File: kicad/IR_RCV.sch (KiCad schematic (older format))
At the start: 15 parts, among them P5 PR_Host, P6 PR_Slave, Q1 DMN3065LW-7, U6 TLV316IDCKR

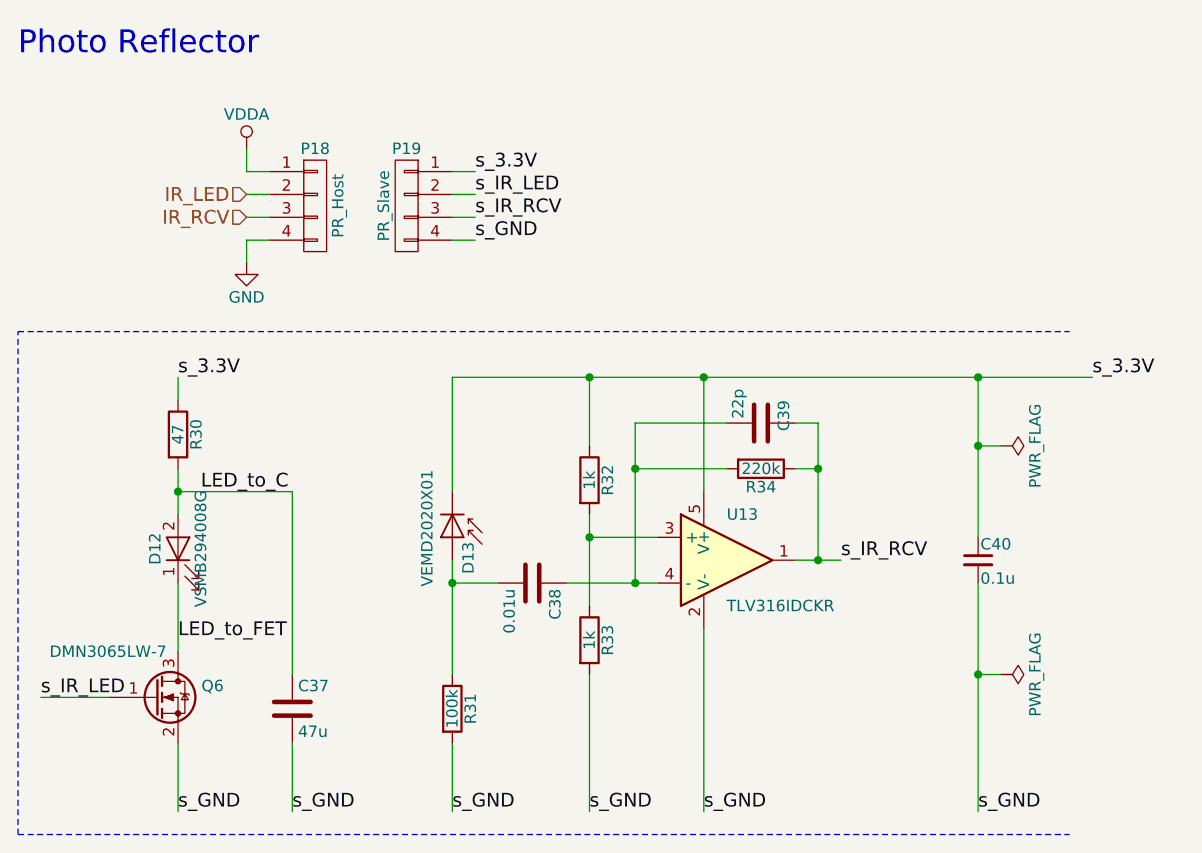
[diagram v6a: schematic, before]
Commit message: 実装経験をもとにフットプリントを改良，ミスを修正
SC70サイズのオペアンプのピンアサインを修正
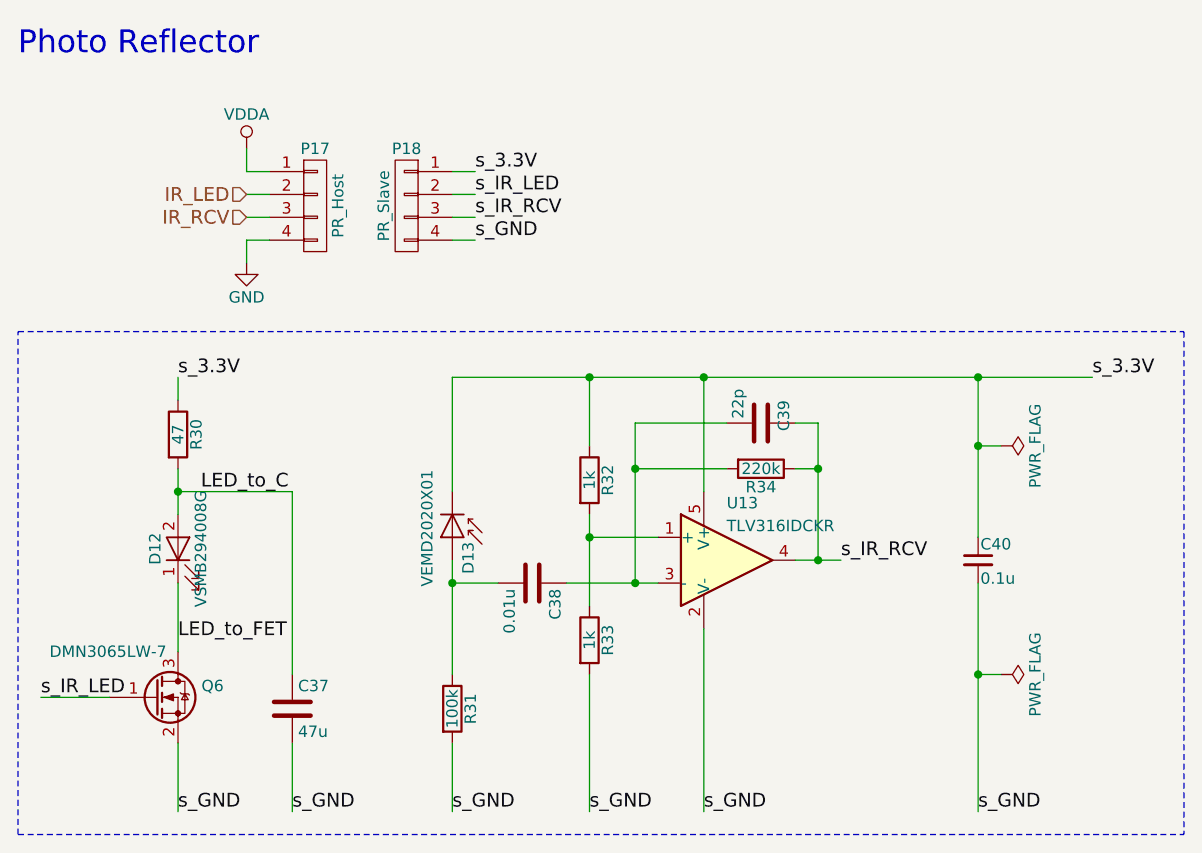
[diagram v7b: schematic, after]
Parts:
- removed U6: TLV316IDCKR, TO_SOT_Packages_SMD:SOT-353_SC-70-5, symbol MCP6L91
- added U6: TLV316IDCKR, TO_SOT_Packages_SMD:SOT-353_SC-70-5, symbol OPA333DCK
- renumbered P5 to P4, P6 to P5
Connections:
- net s_3.3V: now also U6.5 (V+)
- net s_GND: now also U6.2 (V-)
- net s_IR_RCV: now also U6.4
- net at C20.1, C21.2, R10.2: now also U6.3 (-)
- net at R8.2, R9.1: now also U6.1 (+)
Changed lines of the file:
@@
 Photo Reflector
 $Comp
-L CONN_01X04 P6
+L CONN_01X04 P5
 U 1 1 589BE652
 P 5400 2550
-AR Path="/57CF0B09/589BE652" Ref="P6"  Part="1"
-AR Path="/57CF2A30/589BE652" Ref="P8"  Part="1"
-AR Path="/597E1B35/589BE652" Ref="P17"  Part="1"
-AR Path="/597E1B39/589BE652" Ref="P19"  Part="1"
-F 0 "P19" H 5400 2800 50  0000 C CNN
+AR Path="/57CF0B09/589BE652" Ref="P5"  Part="1"
+AR Path="/57CF2A30/589BE652" Ref="P7"  Part="1"
+AR Path="/597E1B35/589BE652" Ref="P16"  Part="1"
+AR Path="/597E1B39/589BE652" Ref="P18"  Part="1"
+F 0 "P18" H 5400 2800 50  0000 C CNN
 F 1 "PR_Slave" V 5500 2550 50  0000 C CNN
 F 2 "mouse:STAND_PR_SLAVE" H 5400 2550 50  0001 C CNN
@@
 s_IR_LED
 $Comp
-L CONN_01X04 P5
+L CONN_01X04 P4
 U 1 1 589BE88F
 P 5000 2550
-AR Path="/57CF0B09/589BE88F" Ref="P5"  Part="1"
-AR Path="/57CF2A30/589BE88F" Ref="P7"  Part="1"
-AR Path="/597E1B35/589BE88F" Ref="P16"  Part="1"
-AR Path="/597E1B39/589BE88F" Ref="P18"  Part="1"
-F 0 "P18" H 5000 2800 50  0000 C CNN
+AR Path="/57CF0B09/589BE88F" Ref="P4"  Part="1"
+AR Path="/57CF2A30/589BE88F" Ref="P6"  Part="1"
+AR Path="/597E1B35/589BE88F" Ref="P15"  Part="1"
+AR Path="/597E1B39/589BE88F" Ref="P17"  Part="1"
+F 0 "P17" H 5000 2800 50  0000 C CNN
 F 1 "PR_Host" V 5100 2550 50  0000 C CNN
 F 2 "mouse:STAND_PR_HOST" H 5000 2550 50  0001 C CNN
@@
 IR_LED
 $Comp
-L GND #PWR043
+L GND #PWR42
 U 1 1 589BF265
 P 4700 2800
-AR Path="/57CF0B09/589BF265" Ref="#PWR043"  Part="1"
-AR Path="/57CF2A30/589BF265" Ref="#PWR047"  Part="1"
-AR Path="/597E1B35/589BF265" Ref="#PWR080"  Part="1"
-AR Path="/597E1B39/589BF265" Ref="#PWR084"  Part="1"
-F 0 "#PWR084" H 4700 2550 50  0001 C CNN
+AR Path="/57CF0B09/589BF265" Ref="#PWR42"  Part="1"
+AR Path="/57CF2A30/589BF265" Ref="#PWR44"  Part="1"
+AR Path="/597E1B35/589BF265" Ref="#PWR69"  Part="1"
+AR Path="/597E1B39/589BF265" Ref="#PWR71"  Part="1"
+F 0 "#PWR71" H 4700 2550 50  0001 C CNN
 F 1 "GND" H 4700 2650 50  0000 C CNN
 F 2 "" H 4700 2800 50  0000 C CNN
@@
 	3700 5300 3700 3100
 Wire Notes Line
-	3700 5300 8300 5300
+	3700 5300 8800 5300
 Wire Notes Line
-	3700 3100 8300 3100
+	3700 3100 8800 3100
 Wire Wire Line
 	5600 4900 5600 5200
@@
 	7900 4000 7900 3300
 Connection ~ 7900 3300
-$Comp
-L MCP6L91 U6
-U 1 1 594AC13D
-P 6800 4100
-AR Path="/57CF0B09/594AC13D" Ref="U6"  Part="1"
-AR Path="/57CF2A30/594AC13D" Ref="U7"  Part="1"
-AR Path="/597E1B35/594AC13D" Ref="U12"  Part="1"
-AR Path="/597E1B39/594AC13D" Ref="U13"  Part="1"
-F 0 "U13" H 6800 4300 50  0000 L CNN
-F 1 "TLV316IDCKR" H 6800 3900 50  0000 L CNN
-F 2 "TO_SOT_Packages_SMD:SOT-353_SC-70-5" H 6800 3700 50  0001 C CNN
-F 3 "" H 6800 4300 50  0001 C CNN
-	1    6800 4100
-	1    0    0    -1
-$EndComp
 $Comp
 L D_Photo D3
@@
 $EndComp
 $Comp
-L PWR_FLAG #FLG044
+L PWR_FLAG #FLG3
 U 1 1 594B7401
 P 8000 3600
-AR Path="/57CF0B09/594B7401" Ref="#FLG044"  Part="1"
-AR Path="/57CF2A30/594B7401" Ref="#FLG048"  Part="1"
-AR Path="/597E1B35/594B7401" Ref="#FLG081"  Part="1"
-AR Path="/597E1B39/594B7401" Ref="#FLG085"  Part="1"
-F 0 "#FLG085" H 8000 3675 50  0001 C CNN
+AR Path="/57CF0B09/594B7401" Ref="#FLG3"  Part="1"
+AR Path="/57CF2A30/594B7401" Ref="#FLG5"  Part="1"
+AR Path="/597E1B35/594B7401" Ref="#FLG13"  Part="1"
+AR Path="/597E1B39/594B7401" Ref="#FLG15"  Part="1"
+F 0 "#FLG15" H 8000 3675 50  0001 C CNN
 F 1 "PWR_FLAG" H 8000 3750 50  0000 C CNN
 F 2 "" H 8000 3600 50  0001 C CNN
@@
 $EndComp
 $Comp
-L PWR_FLAG #FLG045
+L PWR_FLAG #FLG4
 U 1 1 594B744C
 P 8000 4600
-AR Path="/57CF0B09/594B744C" Ref="#FLG045"  Part="1"
-AR Path="/57CF2A30/594B744C" Ref="#FLG049"  Part="1"
-AR Path="/597E1B35/594B744C" Ref="#FLG082"  Part="1"
-AR Path="/597E1B39/594B744C" Ref="#FLG086"  Part="1"
-F 0 "#FLG086" H 8000 4675 50  0001 C CNN
+AR Path="/57CF0B09/594B744C" Ref="#FLG4"  Part="1"
+AR Path="/57CF2A30/594B744C" Ref="#FLG6"  Part="1"
+AR Path="/597E1B35/594B744C" Ref="#FLG14"  Part="1"
+AR Path="/597E1B39/594B744C" Ref="#FLG16"  Part="1"
+F 0 "#FLG16" H 8000 4675 50  0001 C CNN
 F 1 "PWR_FLAG" H 8000 4750 50  0000 C CNN
 F 2 "" H 8000 4600 50  0001 C CNN
@@
 Connection ~ 7900 3600
 $Comp
-L VDDA #PWR046
+L VDDA #PWR41
 U 1 1 59C54857
 P 4700 2300
-AR Path="/57CF0B09/59C54857" Ref="#PWR046"  Part="1"
-AR Path="/57CF2A30/59C54857" Ref="#PWR050"  Part="1"
-AR Path="/597E1B35/59C54857" Ref="#PWR083"  Part="1"
-AR Path="/597E1B39/59C54857" Ref="#PWR087"  Part="1"
-F 0 "#PWR087" H 4700 2150 50  0001 C CNN
+AR Path="/57CF0B09/59C54857" Ref="#PWR41"  Part="1"
+AR Path="/57CF2A30/59C54857" Ref="#PWR43"  Part="1"
+AR Path="/597E1B35/59C54857" Ref="#PWR68"  Part="1"
+AR Path="/597E1B39/59C54857" Ref="#PWR70"  Part="1"
+F 0 "#PWR70" H 4700 2150 50  0001 C CNN
 F 1 "VDDA" H 4700 2450 50  0000 C CNN
 F 2 "" H 4700 2300 50  0001 C CNN
@@
 	1    0    0    -1
 $EndComp
+$Comp
+L OPA333DCK U6
+U 1 1 59F29D23
+P 6800 4100
+AR Path="/57CF0B09/59F29D23" Ref="U6"  Part="1"
+AR Path="/57CF2A30/59F29D23" Ref="U7"  Part="1"
+AR Path="/597E1B35/59F29D23" Ref="U12"  Part="1"
+AR Path="/597E1B39/59F29D23" Ref="U13"  Part="1"
+F 0 "U13" H 6800 4350 50  0000 L CNN
+F 1 "TLV316IDCKR" H 6800 4250 50  0000 L CNN
+F 2 "TO_SOT_Packages_SMD:SOT-353_SC-70-5" H 6800 3950 50  0001 L CNN
+F 3 "" H 6950 4250 50  0001 C CNN
+	1    6800 4100
+	1    0    0    -1
+$EndComp
+Wire Notes Line
+	8800 3100 8800 5300
 $EndSCHEMATC
